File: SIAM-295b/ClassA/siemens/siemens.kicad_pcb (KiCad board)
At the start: 2 copper layers, 107 parts, among them J1 PWR_IN, J2 Conn_01x08_Pin, J3 AUDIO_IN, J4 AUDIO_OUT, Q1 BC549, Q10 BD139, Q11 BD139, Q12 BC549, Q2 BD139, Q3 BD139, Q4 BC549, Q5 BC549, Q6 BD139, Q7 BD139, Q8 BC549, Q9 BC549, SW1 SW_Rotary_2x6, SW2 SW_DPDT_x2

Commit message: update pcb
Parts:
- moved RV18 111.5 mm to (213.2, 51.2), turned to -90 degrees
- moved R8 106.8 mm to (213.0, 68.8), turned to 180 degrees
- moved R21 102.9 mm to (196.6, 26.4), turned to -90 degrees
- moved R10 100.5 mm to (203.8, 64.5), turned to 180 degrees
- moved R23 100.1 mm to (202.7, 124.2)
- moved R17 97.5 mm to (214.8, 90.0), turned to 180 degrees
- moved R11 96.1 mm to (196.2, 60.2)
- moved R15 93.4 mm to (207.2, 96.8)
- moved R37 93.1 mm to (215.2, 111.0), turned to 180 degrees
- moved C10 93.0 mm to (107.8, 44.8), turned to -90 degrees
- moved R34 92.8 mm to (210.1, 134.0), turned to 180 degrees
- moved R14 92.7 mm to (203.2, 101.5), turned to 180 degrees
- moved R33 92.7 mm to (210.3, 129.2), turned to 180 degrees
- moved R13 89.8 mm to (203.2, 89.2), turned to 180 degrees
- moved R9 87.6 mm to (193.0, 70.0), turned to 180 degrees
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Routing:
- net Net-(J4-Pin_1): track 0.00 -> 104.9 mm
- net +24V: track 0.00 -> 85.1 mm
- net Net-(Q11-B): track 0.00 -> 54.6 mm, vias 0 -> 2
- net Net-(C4-Pad1): track 0.00 -> 53.7 mm
- net Net-(Q10-C): track 0.00 -> 43.4 mm, vias 0 -> 2
- net Net-(Q6-C): track 0.00 -> 43.3 mm
- net Net-(Q7-C): track 0.00 -> 36.5 mm
- net Net-(Q12-E): track 0.00 -> 33.4 mm
- net Net-(Q6-B): track 0.00 -> 31.6 mm
- net Net-(C15-Pad2): track 0.00 -> 28.3 mm
- net Net-(Q5-C): track 0.00 -> 22.4 mm
- net Net-(C34-Pad2): track 0.00 -> 20.9 mm
- net Net-(Q11-E): track 0.00 -> 20.7 mm
- net Net-(Q8-B): track 0.00 -> 19.9 mm
- net Net-(Q8-C): track 0.00 -> 16.9 mm
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- added copper zone on B.Cu, net GND

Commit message: Update siemens.kicad_pcb
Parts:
- moved TP1 150.1 mm to (172.8, 53.2)
- moved R53 99.1 mm to (107.4, 64.2), turned to 180 degrees
- moved C32 94.2 mm to (109.9, 68.9), turned to -90 degrees
- moved C26 94.2 mm to (133.2, 75.7)
- moved R52 92.1 mm to (118.1, 64.4), turned to 180 degrees
- moved R3 91.9 mm to (119.4, 69.2), turned to 0 degrees
- moved R50 89.2 mm to (118.7, 59.2), turned to 180 degrees
- moved R5 88.2 mm to (127.9, 64.2), turned to 0 degrees
- moved R54 86.9 mm to (124.7, 76.4), turned to 180 degrees
- moved C31 86.6 mm to (102.9, 76.2), turned to 90 degrees
- moved R2 82.6 mm to (133.9, 43.4), turned to 180 degrees
- moved TP2 77.9 mm to (121.2, 136.2)
- moved TP4 76.6 mm to (146.5, 135.8)
- moved TP3 72.4 mm to (153.2, 136.2)
- moved R51 72.1 mm to (117.0, 81.4)
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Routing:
- net Net-(Q1-C): track 0.00 -> 64.7 mm
- net +24V: track 85.1 -> 147.6 mm
- net Net-(C10-Pad1): track 0.00 -> 61.6 mm
- net Net-(Q1-B): track 0.00 -> 43.8 mm
- net Net-(C13-Pad1): track 0.00 -> 40.8 mm
- net Net-(C25-Pad2): track 0.00 -> 34.9 mm
- net Net-(Q1-E): track 0.00 -> 29.0 mm
- net Net-(Q3-B): track 0.00 -> 27.4 mm
- net Net-(Q2-E): track 0.00 -> 25.4 mm
- net Net-(Q2-C): track 0.00 -> 25.3 mm
- net Net-(J2-Pin_5): track 0.00 -> 22.1 mm
- net Net-(Q4-B): track 14.1 -> 35.3 mm, vias 0 -> 2
- net Net-(R21-Pad2): track 0.00 -> 20.7 mm
- net Net-(C14-Pad1): track 0.00 -> 19.2 mm
- net Net-(C20-Pad1): track 0.00 -> 17.0 mm
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
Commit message: update pcb
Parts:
- moved R34 86.1 mm to (129.1, 57.0)
- moved C25 76.3 mm to (69.0, 118.2)
- moved Q8 70.7 mm to (125.3, 61.0)
- moved C33 69.3 mm to (114.0, 110.9)
- moved R2 65.6 mm to (177.3, 92.7)
- moved C3 64.4 mm to (168.0, 109.0)
- moved Q9 63.2 mm to (135.6, 61.1)
- moved TP1 62.9 mm to (165.5, 115.7)
- moved R53 62.6 mm to (154.8, 105.0)
- moved J3 62.5 mm to (175.0, 109.0)
- moved RV18 59.6 mm to (161.0, 115.9)
- moved C16 58.7 mm to (129.8, 68.2)
- moved Q10 57.6 mm to (130.7, 53.5)
- moved C10 57.6 mm to (114.0, 101.8)
- moved C1 55.8 mm to (175.0, 101.0)
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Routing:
- net Net-(J4-Pin_1): track 112.0 -> 9.80 mm
- net +24V: track 147.6 -> 74.8 mm
- net Net-(Q12-E): track 33.4 -> 99.8 mm
- net Net-(Q8-C): track 16.9 -> 76.0 mm
- net Net-(C13-Pad1): track 40.8 -> 0.00 mm
- net Net-(Q2-E): track 25.4 -> 59.8 mm
- net Net-(Q3-E): track 4.96 -> 38.4 mm
- net Net-(Q2-C): track 25.3 -> 56.6 mm
- net Net-(Q10-B): track 14.8 -> 44.7 mm
- net Net-(C10-Pad1): track 61.6 -> 32.7 mm
- net Net-(Q4-E): track 12.6 -> 40.5 mm
- net Net-(Q3-B): track 27.4 -> 54.3 mm
- net Net-(C25-Pad2): track 34.9 -> 8.85 mm
- net Net-(Q8-E): track 15.1 -> 40.7 mm
- net Net-(C30-Pad2): track 10.7 -> 34.4 mm, vias 0 -> 2
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
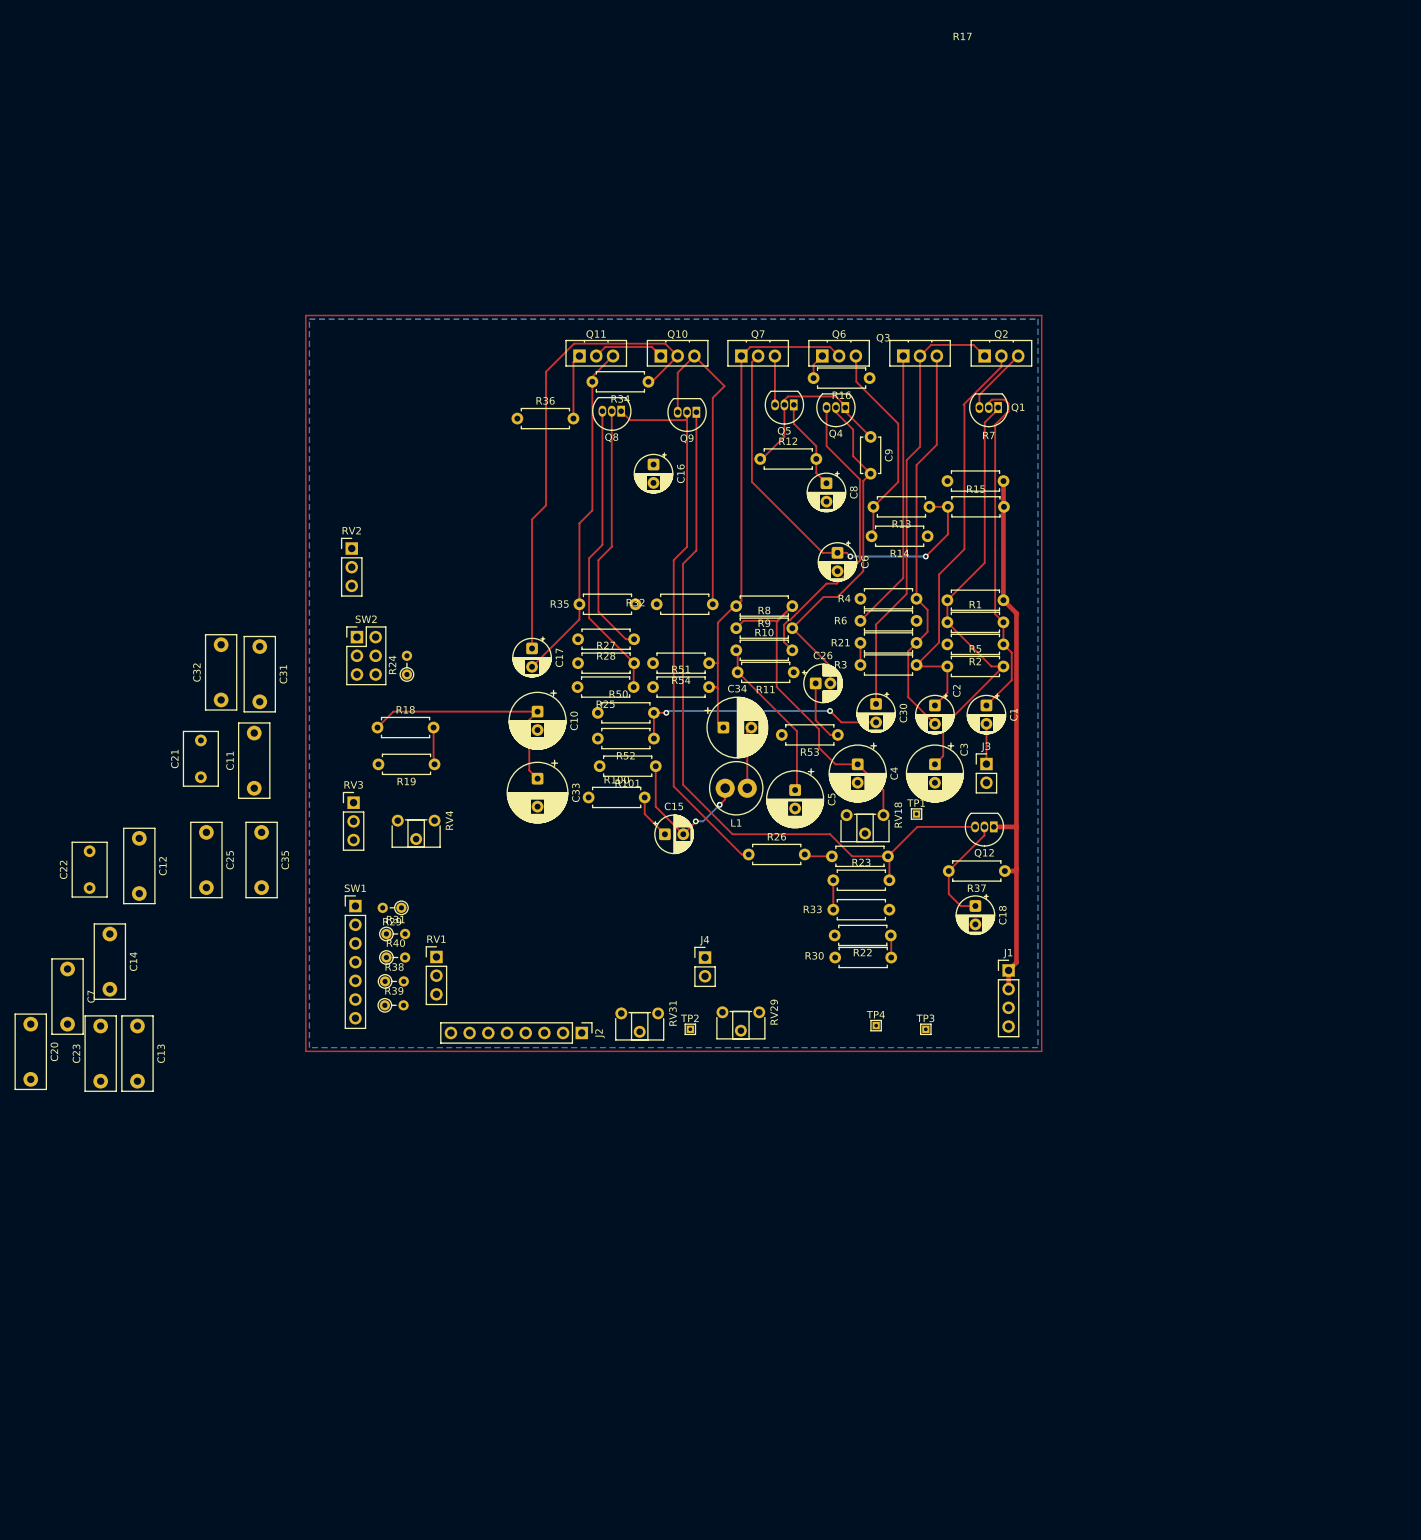
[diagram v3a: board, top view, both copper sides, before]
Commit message: update pcb
switch transistors & resistors to smd
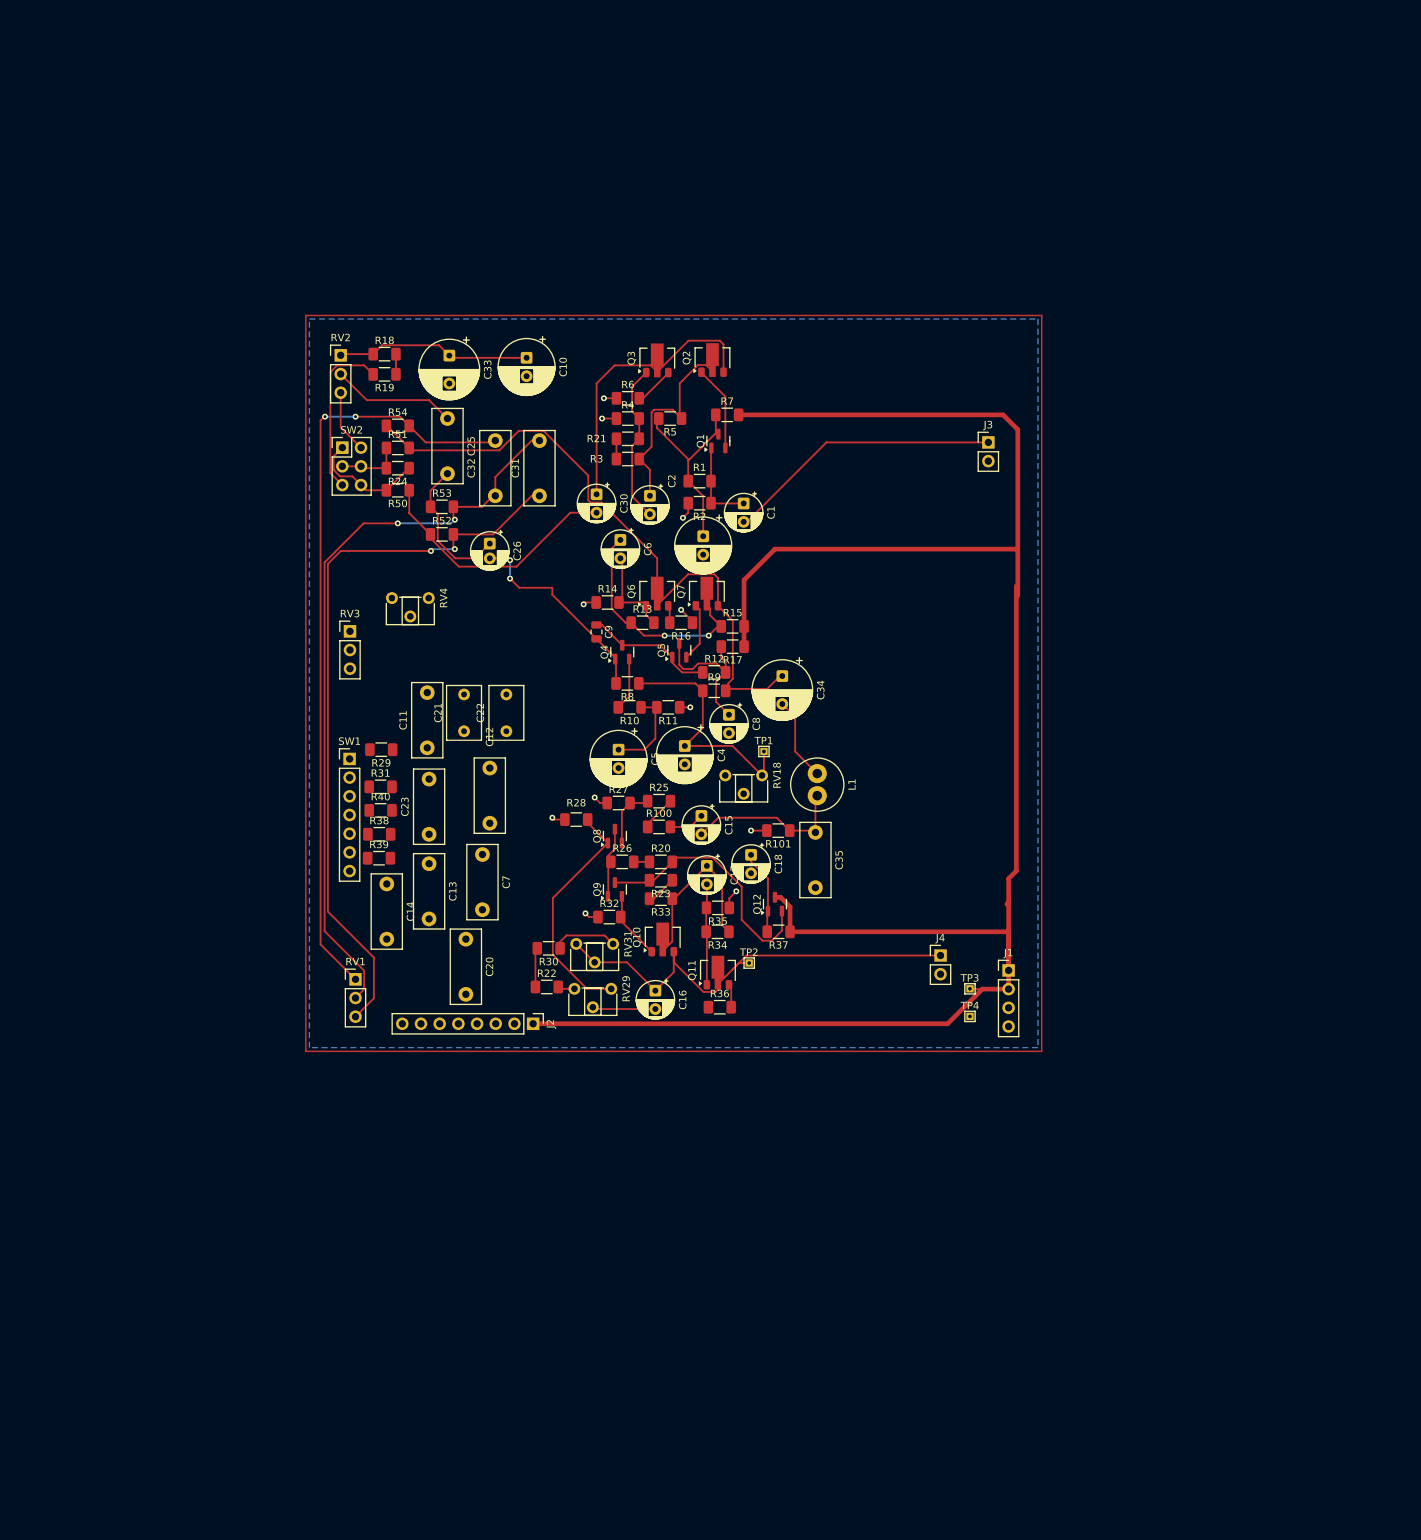
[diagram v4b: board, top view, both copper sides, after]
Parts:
- C9: footprint Capacitor_THT:C_Disc_D4.7mm_W2.5mm_P5.00mm -> Capacitor_SMD:C_0805_2012Metric
- Q1, Q12, Q4, Q5, Q8, Q9: value BC549 -> BC849; footprint Package_TO_SOT_THT:TO-92_Inline -> Package_TO_SOT_SMD:SOT-23
- Q10, Q11, Q2, Q3, Q6, Q7: value BD139 -> BCX56; footprint Package_TO_SOT_THT:TO-126-3_Vertical -> Package_TO_SOT_SMD:SOT-89-3
- R1, R10, R100, R101, R11, R12, R13, R14, R15, R16, R17, R18, R19, R2, R20, R21, R22, R23, R25, R26, R27, R28, R3, R30, R32, R33, R34, R35, R36, R37, R4, R5, R50, R51, R52, R53, R54, R6, R7, R8, R9: footprint Resistor_THT:R_Axial_DIN0207_L6.3mm_D2.5mm_P7.62mm_Horizontal -> Resistor_SMD:R_1206_3216Metric_Pad1.30x1.75mm_HandSolder
- R24, R29, R31, R38, R39, R40: footprint Resistor_THT:R_Axial_DIN0204_L3.6mm_D1.6mm_P2.54mm_Vertical -> Resistor_SMD:R_1206_3216Metric_Pad1.30x1.75mm_HandSolder
- moved Q11 85.6 mm to (138.5, 137.0), turned to 90 degrees
- moved R36 84.6 mm to (138.8, 142.0)
- moved Q10 79.0 mm to (131.0, 132.5), turned to 90 degrees
- moved R34 75.3 mm to (138.4, 131.8)
- moved C35 75.3 mm to (151.8, 118.2)
- moved C16 71.5 mm to (130.0, 139.8)
- moved Q9 65.8 mm to (124.5, 126.0), turned to 90 degrees
- moved C25 65.1 mm to (101.8, 62.0)
- moved R53 62.1 mm to (101.0, 74.0), turned to 0 degrees
- moved C22 60.5 mm to (109.8, 104.5)
- moved C20 60.2 mm to (104.2, 132.8)
- moved C33 58.7 mm to (102.0, 53.4)
- moved C7 58.5 mm to (106.5, 121.2)
- moved Q8 57.7 mm to (124.5, 118.8), turned to 90 degrees
- moved C23 55.8 mm to (99.2, 118.5)
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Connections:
- Q1 pad 1: Net-(Q1-C) -> Net-(Q1-B)
- Q1 pad 2: Net-(Q1-B) -> Net-(Q1-E)
- Q1 pad 3: Net-(Q1-E) -> Net-(Q1-C)
- Q10 pad 1: Net-(J4-Pin_1) -> Net-(Q10-B)
- Q10 pad 3: Net-(Q10-B) -> Net-(J4-Pin_1)
- Q11 pad 1: Net-(Q11-E) -> Net-(Q11-B)
- Q11 pad 3: Net-(Q11-B) -> Net-(Q11-E)
- Q12 pad 1: +24V -> Net-(Q12-B)
- Q12 pad 2: Net-(Q12-B) -> Net-(Q12-E)
- Q12 pad 3: Net-(Q12-E) -> +24V
- Q2 pad 1: Net-(Q2-E) -> Net-(Q1-E)
- Q2 pad 3: Net-(Q1-E) -> Net-(Q2-E)
- Q3 pad 1: Net-(Q3-E) -> Net-(Q3-B)
- Q3 pad 3: Net-(Q3-B) -> Net-(Q3-E)
- Q4 pad 1: Net-(Q4-C) -> Net-(Q4-B)
- Q4 pad 2: Net-(Q4-B) -> Net-(Q4-E)
- Q4 pad 3: Net-(Q4-E) -> Net-(Q4-C)
- Q5 pad 1: Net-(Q5-C) -> Net-(Q4-C)
- Q5 pad 2: Net-(Q4-C) -> Net-(Q5-E)
- Q5 pad 3: Net-(Q5-E) -> Net-(Q5-C)
- Q6 pad 1: Net-(Q6-E) -> Net-(Q6-B)
- Q6 pad 3: Net-(Q6-B) -> Net-(Q6-E)
- Q7 pad 1: Net-(Q6-C) -> Net-(Q5-E)
- Q7 pad 3: Net-(Q5-E) -> Net-(Q6-C)
- Q8 pad 1: Net-(Q8-C) -> Net-(Q8-B)
- Q8 pad 2: Net-(Q8-B) -> Net-(Q8-E)
- Q8 pad 3: Net-(Q8-E) -> Net-(Q8-C)
- Q9 pad 1: Net-(Q12-E) -> Net-(Q8-C)
- Q9 pad 2: Net-(Q8-C) -> Net-(Q10-B)
- Q9 pad 3: Net-(Q10-B) -> Net-(Q12-E)
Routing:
- net +24V: track 74.8 -> 277.9 mm
- net Net-(C32-Pad2): track 0.00 -> 103.8 mm, vias 0 -> 2
- net Net-(C31-Pad2): track 0.00 -> 100.8 mm, vias 0 -> 2
- net Net-(C31-Pad1): track 0.00 -> 99.2 mm, vias 0 -> 2
- net Net-(Q8-C): track 76.0 -> 9.52 mm
- net Net-(Q12-E): track 99.8 -> 34.6 mm
- net Net-(J4-Pin_1): track 9.80 -> 64.3 mm
- net Net-(Q10-C): track 63.5 -> 24.4 mm
- net Net-(Q1-B): track 47.9 -> 12.4 mm
- net Net-(Q10-B): track 44.7 -> 9.31 mm
- net Net-(Q4-E): track 40.5 -> 7.18 mm
- net Net-(Q3-E): track 38.4 -> 5.44 mm
- net Net-(Q3-B): track 54.3 -> 21.9 mm
- net Net-(Q8-E): track 40.7 -> 8.40 mm
- net Net-(Q11-B): track 46.0 -> 13.7 mm
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
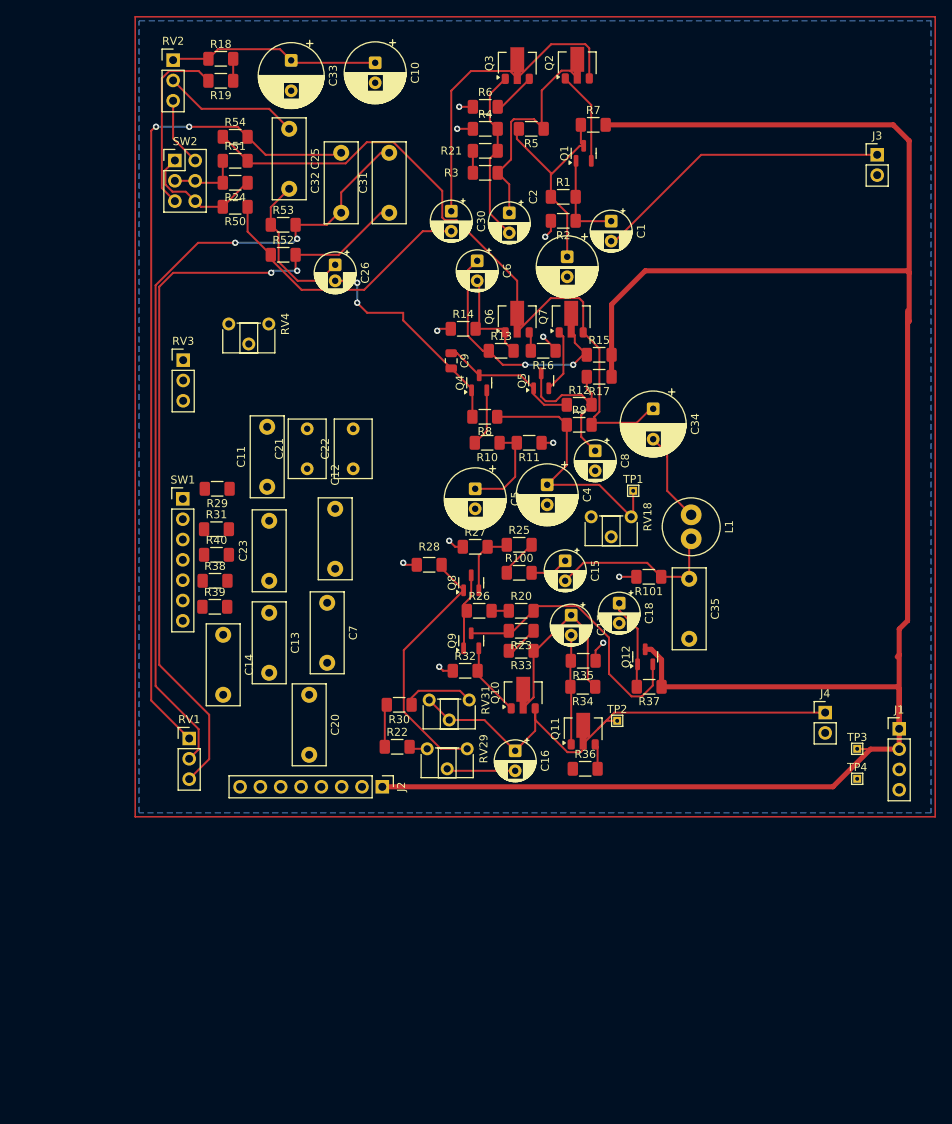
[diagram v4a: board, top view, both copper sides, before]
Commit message: update pcb
successfully routed all components
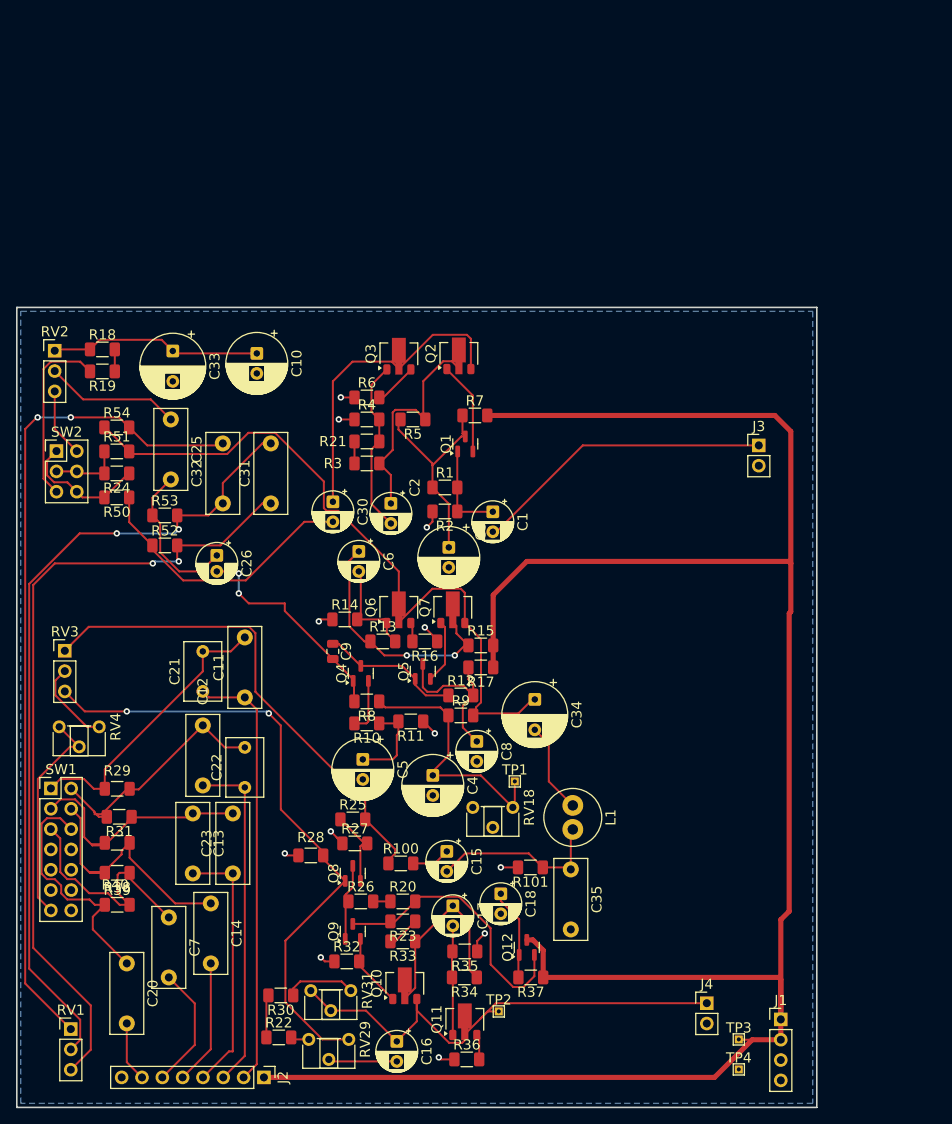
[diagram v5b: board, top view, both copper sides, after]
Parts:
- SW1: footprint Connector_PinHeader_2.54mm:PinHeader_1x07_P2.54mm_Vertical -> Connector_PinHeader_2.54mm:PinHeader_2x07_P2.54mm_Vertical
- moved RV4 54.6 mm to (78.0, 136.8)
- moved C7 44.0 mm to (86.7, 160.6)
- moved C22 42.1 mm to (96.2, 144.3)
- moved C20 40.6 mm to (81.5, 166.3)
- moved R25 40.1 mm to (109.7, 148.3)
- moved R27 40.0 mm to (110.0, 151.3)
- moved SW1 39.8 mm to (72.0, 144.5)
- moved R29 39.5 mm to (80.2, 144.5)
- moved C17 39.2 mm to (122.2, 159.1)
- moved C18 39.2 mm to (128.2, 157.6)
- moved C30 39.2 mm to (107.2, 108.6)
- moved Q1 39.2 mm to (123.8, 101.4)
- moved R21 39.2 mm to (111.5, 101.1)
- moved R3 39.2 mm to (111.5, 103.8)
- moved C2 39.2 mm to (114.5, 108.8)
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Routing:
- net Net-(R100-Pad1): track 4.78 -> 61.4 mm
- net Net-(J2-Pin_2): track 0.00 -> 54.4 mm
- net Net-(Q8-B): track 32.4 -> 78.8 mm, vias 0 -> 2
- net Net-(J2-Pin_3): track 0.00 -> 42.4 mm
- net Net-(C11-Pad2): track 0.00 -> 36.0 mm
- net Net-(J2-Pin_4): track 0.00 -> 32.3 mm
- net Net-(C14-Pad1): track 0.00 -> 31.9 mm
- net Net-(C20-Pad1): track 0.00 -> 30.6 mm
- net Net-(C12-Pad1): track 0.00 -> 30.2 mm
- net Net-(C13-Pad1): track 0.00 -> 29.6 mm
- net Net-(C7-Pad1): track 0.00 -> 29.1 mm
- net Net-(RV4-Pad2): track 0.00 -> 27.5 mm
- net Net-(J2-Pin_5): track 0.00 -> 15.7 mm
- net Net-(J2-Pin_6): track 0.00 -> 15.5 mm
- net Net-(RV3-Pad2): track 0.00 -> 10.6 mm
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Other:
- board outline added: 100 x 100 mm
